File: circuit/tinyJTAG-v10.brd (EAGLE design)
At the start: 32.4 x 12.2 mm, 16 parts, among them IC1 TINY85S, IC2 74125SOIC14, Q2 MMBT3906LT1SMD, X1 USBPCB

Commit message: added CC info back
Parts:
- added U$4: CREATIVE_COMMONS, SparkFun:CREATIVE_COMMONS
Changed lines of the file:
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@@
 <layer number="223" name="223bmp" color="24" fill="1" visible="no" active="no"/>
 <layer number="224" name="224bmp" color="25" fill="1" visible="no" active="no"/>
+<layer number="250" name="Descript" color="3" fill="1" visible="no" active="no"/>
 <layer number="251" name="SMDround" color="12" fill="11" visible="no" active="no"/>
 <layer number="254" name="cooling" color="7" fill="1" visible="no" active="yes"/>
@@
 <element name="R5" library="SparkFun" package="0603-RES" value="" x="8.128" y="1.7145" rot="R270"/>
 <element name="C2" library="rcl" package="C0805" value="10uF" x="22.1615" y="9.652" rot="R270"/>
+<element name="U$4" library="SparkFun" package="CREATIVE_COMMONS" value="CREATIVE_COMMONS" x="14.1605" y="-20.955"/>
 </elements>
 <signals>

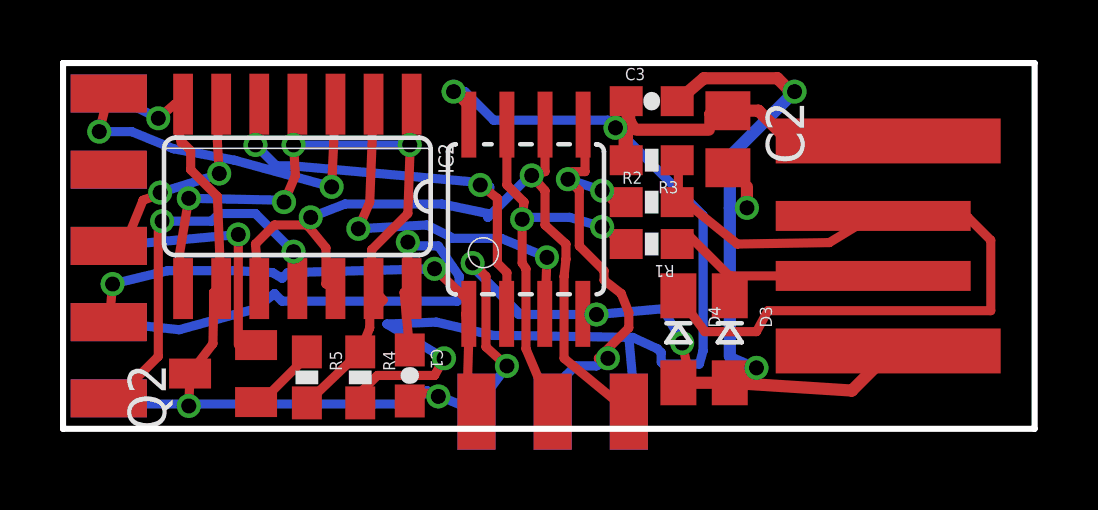
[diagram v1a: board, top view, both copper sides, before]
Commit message: Version sent for manufacturing initial prototypes
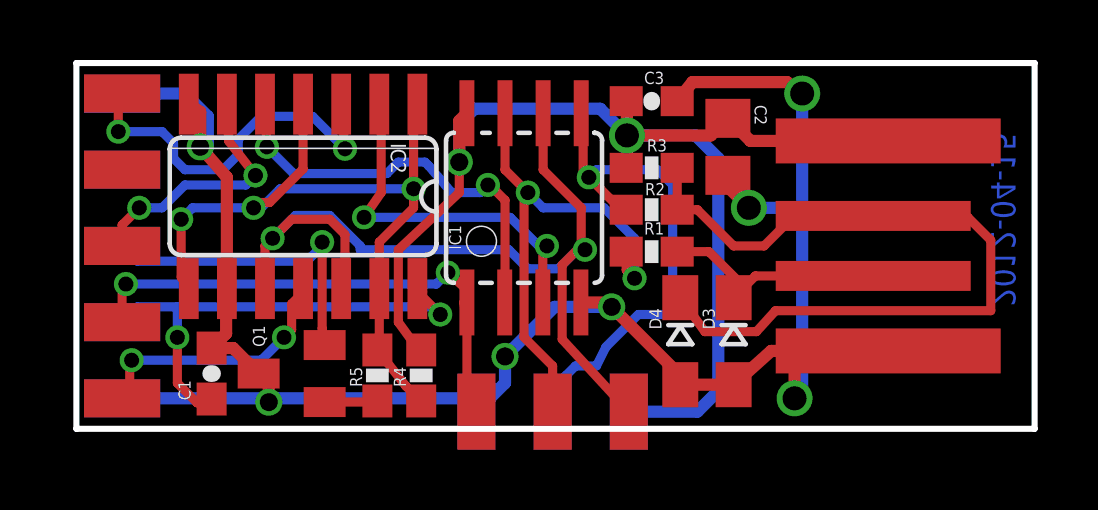
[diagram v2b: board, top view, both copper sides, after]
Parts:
- removed Q2: MMBT3906LT1SMD, transistor-pnp:SOT23-BEC
- removed U$4: CREATIVE_COMMONS, SparkFun:CREATIVE_COMMONS
- added LOGO1: OSHW_LOGO_FILLX0150-NT, ohw-logo:OSHW_FILLX150_NOTEXT
- added Q1: MMBT3906LT1SMD, transistor-pnp:SOT23-BEC
- moved C1 6.60 mm to (4.95, 1.84), turned to 90 degrees
- moved R5 2.35 mm to (10.5, 1.78), turned to 90 degrees
- moved R4 2.03 mm to (11.9, 1.78), turned to 90 degrees
- moved U$1 0.44 mm to (1.97, 6.10)
- moved IC1 0.39 mm to (15.4, 7.37)
- moved R1 0.25 mm to (19.6, 5.91)
- moved C2 0.25 mm to (22.2, 9.40)
- moved R2 0.25 mm to (19.6, 7.30)
- moved R3 0.25 mm to (19.6, 8.70)
- moved IC2 0.19 mm to (8.00, 7.75)
- moved D3 0.14 mm to (22.4, 2.92)
- moved D4 0.09 mm to (20.6, 2.92)
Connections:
- net GND: now also Q1.C; no longer Q2.C
- net N$3: now also Q1.E; no longer Q2.E
- net N$4: now also Q1.B; no longer Q2.B
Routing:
- net GND: track 73.7 -> 67.6 mm, vias 9 -> 7
- net VCC: track 49.7 -> 43.9 mm, vias 3 -> 2
- net TCK: track 13.1 -> 8.83 mm
- net TCK_LOCAL: track 26.1 -> 29.8 mm
- net D+: track 13.8 -> 17.2 mm
- net VCCTARG: track 19.1 -> 16.2 mm, vias 1 -> 2
- net D-: track 15.0 -> 17.2 mm, vias 3 -> 1
- net N$3: track 8.74 -> 10.7 mm
- net TMS: track 7.60 -> 8.99 mm
- net N$4: track 2.96 -> 1.77 mm
- net USB-D-: track 27.6 -> 26.7 mm
- net USB-D+: track 8.56 -> 7.86 mm
- net TDI: track 12.1 -> 12.7 mm
- net N$1: track 26.6 -> 26.3 mm, vias 4 -> 3
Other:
- board size 32.4 x 12.2 mm -> 31.9 x 12.2 mm
- board text added: "2012-04-15"
- board text added: "Altered by Embedded Creations (Louis Beaudoin)"
- board text added: "Creations"
- board text added: "Embedded"
- board text added: "Programmer"
- board text added: "Seeed# 49009"
- board text added: "Tiny AVR JTAG"
- board text removed: "tinyJTAG"
